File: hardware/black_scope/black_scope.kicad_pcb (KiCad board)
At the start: 4 copper layers, 87 x 59 mm, 73 parts, among them J1 Conn_ARM_JTAG_SWD_10, J3 Conn_01x02, J4 Conn_02x04_Odd_Even, J5 Conn_02x02_Odd_Even, P1 USB_C_Plug_USB2.0, Q1 S8050, SW1 SW_Push, SW2 SW_Push, U1 MCP73831-2-OT, U2 XC6206PxxxMR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

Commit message: - Added images
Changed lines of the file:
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@@
   (gr_rect (start 100 75) (end 183 130) (layer "B.SilkS") (width 0.15) (fill none))
   (gr_rect (start 183 75) (end 167 130) (layer "B.SilkS") (width 0.15) (fill none))
+  (gr_rect (start 185 79) (end 151 132) (layer "F.SilkS") (width 0.15) (fill none))
+  (gr_circle (center 181 77) (end 179 77) (layer "F.SilkS") (width 0.15) (fill none))
+  (gr_rect (start 120.5 115) (end 131.5 119) (layer "F.SilkS") (width 0.15) (fill none))
+  (gr_circle (center 161 77) (end 159 77) (layer "F.SilkS") (width 0.15) (fill none))
+  (gr_circle (center 149 84) (end 147 84) (layer "F.SilkS") (width 0.15) (fill none))
+  (gr_rect (start 124.5 115) (end 127.5 120) (layer "F.SilkS") (width 0.15) (fill none))
+  (gr_circle (center 149 119) (end 147 119) (layer "F.SilkS") (width 0.15) (fill none))
   (gr_line (start 185 130) (end 185 126) (layer "Edge.Cuts") (width 0.1))
   (gr_arc (start 185 130) (mid 184.414214 131.414214) (end 183 132) (layer "Edge.Cuts") (width 0.1))

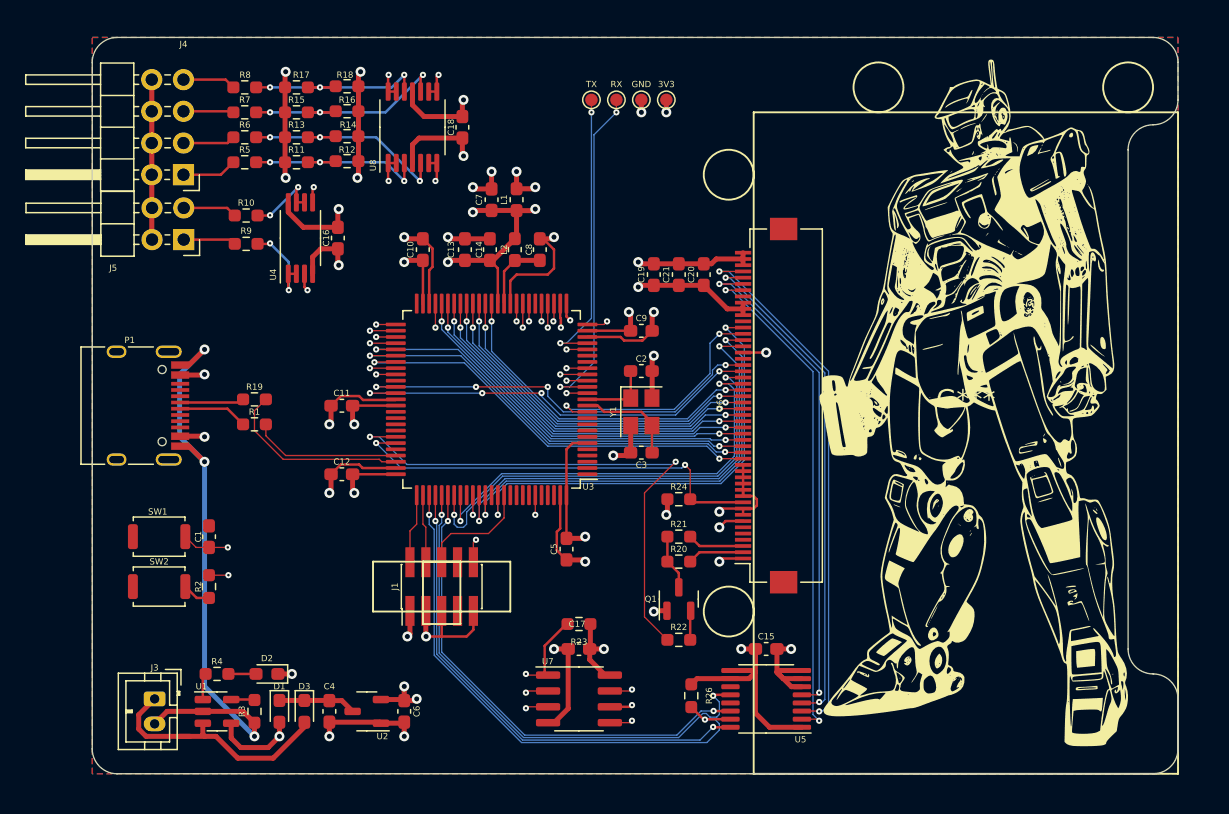
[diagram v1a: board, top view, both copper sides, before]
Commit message: - Fix PCB issues - Add datasheets
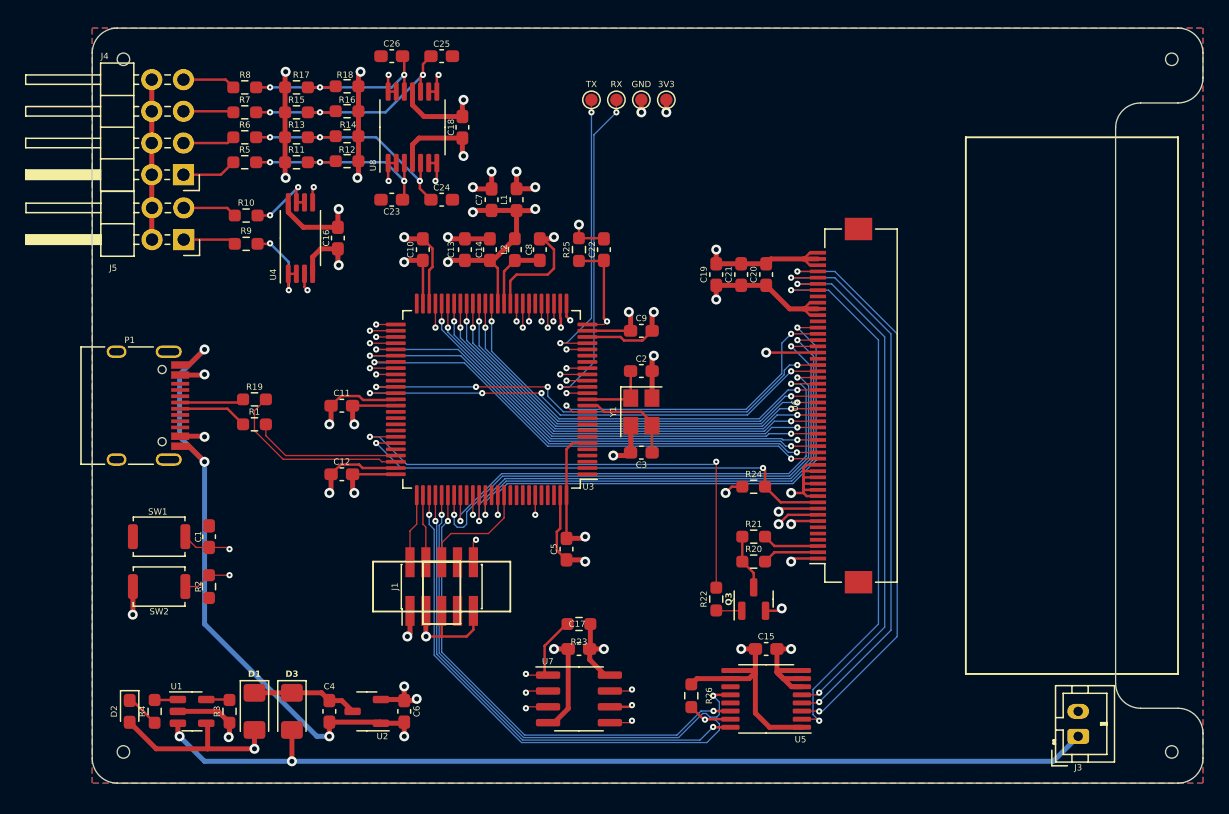
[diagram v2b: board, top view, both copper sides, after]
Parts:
- removed G***: LOGO, LOGO
- removed Q1: S8050, Package_TO_SOT_SMD:SOT-23
- added C22: 100n, Capacitor_SMD:C_0603_1608Metric_Pad1.08x0.95mm_HandSolder, F.Cu at (139.0, 90.0)
- added C23: 100p, Capacitor_SMD:C_0603_1608Metric_Pad1.08x0.95mm_HandSolder, F.Cu at (122.0, 86.0)
- added C24: 100p, Capacitor_SMD:C_0603_1608Metric_Pad1.08x0.95mm_HandSolder, F.Cu at (126.0, 86.0)
- added C25: 100p, Capacitor_SMD:C_0603_1608Metric_Pad1.08x0.95mm_HandSolder, F.Cu at (126.0, 74.5)
- added C26: 100p, Capacitor_SMD:C_0603_1608Metric_Pad1.08x0.95mm_HandSolder, F.Cu at (122.0, 74.5)
- added Q3: Q_NPN_BEC, Package_TO_SOT_SMD:SOT-23, F.Cu at (151.0, 118.0)
- added R25: 10k, Resistor_SMD:R_0603_1608Metric_Pad0.98x0.95mm_HandSolder, F.Cu at (137.0, 90.0)
- C1, C10, C11, C12, C13, C14, C15, C16, C17, C18, C19, C20, C21, C5, C9: value C -> 100n
- C2, C3: value C -> 10p
- C4, C6, C7, C8: value C -> 270n
- D1, D3: footprint Diode_SMD:D_0603_1608Metric_Pad1.05x0.95mm_HandSolder -> Diode_SMD:D_1206_3216Metric_Pad1.42x1.75mm_HandSolder
- L1, L2: value L -> 47u
- R1, R19: value R -> 22
- R10, R20, R21, R9: value R -> 51
- R11, R13, R15, R17: value R -> 2k7
- R12, R14, R16, R18: value R -> 4k3
- R2, R23, R24, R26: value R -> 10k
- R22, R4: value R -> 1k
- R3: value R -> 6.8k
- R5, R6, R7, R8: value R -> 8k2
- moved J3 74.1 mm to (177.0, 129.0), turned to 90 degrees
- moved D2 11.4 mm to (101.0, 127.0), turned to -90 degrees
- moved R24 6.08 mm to (151.0, 109.0)
- moved R20 6.00 mm to (151.0, 115.0)
- moved R21 6.00 mm to (151.0, 113.0)
- moved U6 6.00 mm to (158.0, 102.5)
- moved R4 5.83 mm to (103.0, 127.0), turned to -90 degrees
- moved C19 5.00 mm to (148.0, 92.0)
- moved C20 5.00 mm to (152.0, 92.0)
- moved C21 5.00 mm to (150.0, 92.0)
- moved R22 4.44 mm to (148.0, 118.0), turned to 90 degrees
- moved D1 2.00 mm to (111.0, 127.0)
- moved R3 2.00 mm to (109.0, 127.0)
- moved U1 2.00 mm to (106.0, 127.0)
- moved D3 1.00 mm to (114.0, 127.0)
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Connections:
- D2 pad 1: GND -> Net-(D2-K)
- D2 pad 2: Net-(D2-Pad2) -> VBUS
- R2 pad 1: Net-(R2-Pad1) -> GND
- R4 pad 1: Net-(D2-Pad2) -> Net-(U1-STAT)
- R4 pad 2: Net-(R4-Pad2) -> Net-(D2-K)
- SW2 pad 1: GND -> BOOT0
- SW2 pad 2: Net-(R2-Pad1) -> +3.3V
- U1 pad 1: Net-(R4-Pad2) -> Net-(U1-STAT)
- U6 pad 7: +3.3V -> GND
- U6 pad 8: GND -> +3.3V
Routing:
- net +BATT: track 20.5 -> 77.3 mm, vias 0 -> 2
- net GND: track 201.6 -> 216.3 mm, vias 30 -> 32
- net DAC2_OUT1: track 34.8 -> 41.8 mm
- net +3.3V: track 81.6 -> 88.1 mm, vias 16 -> 17
- net VBUS: track 43.8 -> 50.1 mm
- net FMC_D2: track 36.3 -> 42.3 mm
- net FMC_D14: track 35.2 -> 41.2 mm
- net FMC_A0: track 20.1 -> 26.1 mm
- net FMC_D7: track 28.2 -> 34.2 mm
- net FMC_D6: track 27.8 -> 33.8 mm
- net FMC_D4: track 27.2 -> 33.2 mm
- net FMC_WR: track 36.1 -> 42.1 mm
- net FMC_RD: track 37.3 -> 43.3 mm
- net FMC_D9: track 28.8 -> 34.8 mm
- net FMC_D8: track 28.5 -> 34.5 mm
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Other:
- board size 87 x 59 mm -> 89 x 60.5 mm

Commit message: - Gerber files v2
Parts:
- added C27: 100n, Capacitor_SMD:C_0603_1608Metric_Pad1.08x0.95mm_HandSolder, F.Cu at (159.0, 123.0)
- added C28: 100n, Capacitor_SMD:C_0603_1608Metric_Pad1.08x0.95mm_HandSolder, F.Cu at (159.0, 125.0)
- added C29: 100n, Capacitor_SMD:C_0603_1608Metric_Pad1.08x0.95mm_HandSolder, F.Cu at (159.0, 127.0)
- added C30: 100n, Capacitor_SMD:C_0603_1608Metric_Pad1.08x0.95mm_HandSolder, F.Cu at (159.0, 129.0)
- added D4: D_Schottky_Dual_CommonCathode_AAK_Parallel, Package_TO_SOT_SMD:SOT-23, F.Cu at (112.5, 126.7)
- added G***: LOGO, LOGO, F.Cu at (170.0, 86.0)
- added J2: Conn_02x06_Odd_Even, Connector_PinHeader_2.54mm:PinHeader_2x06_P2.54mm_Vertical_SMD, F.Cu at (104.1, 82.8)
- moved J3 1.83 mm to (175.5, 128.0), turned to 0 degrees
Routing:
- net QSPI_NSS: track 31.4 -> 55.6 mm
- net QSPI_IO1: track 32.9 -> 49.7 mm
- net QSPI_IO2: track 33.2 -> 49.8 mm
- net GND: track 216.3 -> 229.5 mm, vias 32 -> 36
- net QSPI_IO3: track 38.9 -> 49.8 mm
- net QSPI_IO0: track 38.9 -> 49.8 mm
- net YN: track 42.5 -> 45.8 mm
- net QSPI_SCLK: track 47.4 -> 49.9 mm
- net XP: track 45.1 -> 47.5 mm
- net XN: track 45.3 -> 47.7 mm
- net YP: track 46.1 -> 48.1 mm
- net VBUS: track 50.1 -> 51.8 mm
- net +BATT: track 77.3 -> 76.2 mm
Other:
- board text added: "+ -"

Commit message: Long time update
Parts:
- added C31: 270n, Capacitor_SMD:C_0603_1608Metric_Pad1.08x0.95mm_HandSolder, F.Cu at (150.3, 78.9)
- added C32: 270n, Capacitor_SMD:C_0603_1608Metric_Pad1.08x0.95mm_HandSolder, F.Cu at (144.3, 78.9)
- added L3: 47u, Inductor_SMD:L_0603_1608Metric_Pad1.05x0.95mm_HandSolder, F.Cu at (141.3, 76.9)
- added R27: 27, Resistor_SMD:R_0603_1608Metric_Pad0.98x0.95mm_HandSolder, F.Cu at (143.5, 125.5)
- added R28: 27, Resistor_SMD:R_0603_1608Metric_Pad0.98x0.95mm_HandSolder, F.Cu at (143.5, 124.0)
- added R29: 27, Resistor_SMD:R_0603_1608Metric_Pad0.98x0.95mm_HandSolder, F.Cu at (143.5, 128.5)
- added R30: 27, Resistor_SMD:R_0603_1608Metric_Pad0.98x0.95mm_HandSolder, F.Cu at (143.5, 127.0)
- added TP5: TestPoint, TestPoint:TestPoint_Pad_D1.0mm, F.Cu at (136.0, 83.5)
- added TP6: TestPoint, TestPoint:TestPoint_Pad_D1.0mm, F.Cu at (134.0, 83.5)
- added U9: XC6206PxxxMR, Package_TO_SOT_SMD:SOT-23-3, F.Cu at (147.3, 78.9)
- R20, R21: value 51 -> 27
- moved C8 11.2 mm to (132.3, 78.9)
- moved L1 11.1 mm to (141.3, 79.9), turned to 180 degrees
- moved C7 10.9 mm to (138.3, 78.9)
- moved L2 10.7 mm to (135.3, 79.9), turned to 180 degrees
- moved TP1 9.86 mm to (143.0, 86.5)
- moved TP2 9.86 mm to (145.0, 86.5)
- moved TP3 9.86 mm to (147.0, 86.5)
- moved TP4 9.86 mm to (149.0, 86.5)
- moved U6 1.00 mm to (159.0, 102.5)
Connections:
- C13 pad 2: GND -> GNDA
- C14 pad 2: GND -> GNDA
- C16 pad 2: GND -> GNDA
- C18 pad 2: GND -> GNDA
- C22 pad 2: GND -> GNDA
- C23 pad 2: GND -> GNDA
- C24 pad 2: GND -> GNDA
- C25 pad 2: GND -> GNDA
- C26 pad 2: GND -> GNDA
- C7 pad 2: GND -> GNDA
- C8 pad 2: GND -> GNDA
- J2 pad 10: unconnected-(J2-Pin_10-Pad10) -> GNDA
- J2 pad 12: unconnected-(J2-Pin_12-Pad12) -> GNDA
- J2 pad 2: unconnected-(J2-Pin_2-Pad2) -> GNDA
- J2 pad 4: unconnected-(J2-Pin_4-Pad4) -> GNDA
- J2 pad 6: unconnected-(J2-Pin_6-Pad6) -> GNDA
- J2 pad 8: unconnected-(J2-Pin_8-Pad8) -> GNDA
- J4 pad 2: GND -> GNDA
- J4 pad 4: GND -> GNDA
- J4 pad 6: GND -> GNDA
- J4 pad 8: GND -> GNDA
- J5 pad 2: GND -> GNDA
- J5 pad 4: GND -> GNDA
- L1 pad 1: +3.3V -> Net-(U9-VO)
- R12 pad 1: GND -> GNDA
- R14 pad 1: GND -> GNDA
- R16 pad 1: GND -> GNDA
- R18 pad 1: GND -> GNDA
- R25 pad 1: GND -> GNDA
- R26 pad 2: SPI3_NSS -> Net-(U5-~{CS})
- U3 pad 35: GND -> GNDA
- U4 pad 4: GND -> GNDA
- U5 pad 12: SPI3_MISO -> Net-(U5-DOUT)
- U5 pad 14: SPI3_MOSI -> Net-(U5-DIN)
- U5 pad 15: SPI3_NSS -> Net-(U5-~{CS})
- U5 pad 16: SPI3_SCLK -> Net-(U5-DCLK)
- U8 pad 11: GND -> GNDA
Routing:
- net Net-(D1-K): track 8.50 -> 127.2 mm, vias 0 -> 5
- net GNDA: track 0.00 -> 78.0 mm, vias 0 -> 81
- net GND: track 229.5 -> 198.1 mm, vias 36 -> 30
- net VREF: track 5.81 -> 20.2 mm, vias 0 -> 3
- net SPI3_NSS: track 44.7 -> 35.6 mm
- net UART1_RX: track 27.5 -> 21.0 mm
- net +3.3VA: track 39.8 -> 45.7 mm, vias 7 -> 13
- net UART1_TX: track 23.0 -> 17.2 mm
- net Net-(U5-DOUT): track 0.00 -> 5.63 mm
- net Net-(U5-~{CS}): track 0.00 -> 5.27 mm
- net Net-(U5-DIN): track 0.00 -> 5.25 mm
- net SPI3_SCLK: track 39.6 -> 34.8 mm
- net Net-(U5-DCLK): track 0.00 -> 4.82 mm
- net Net-(U9-VO): track 0.00 -> 4.08 mm
- net SPI3_MOSI: track 39.5 -> 36.2 mm
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- added copper zone on In2.Cu, net +3.3V
- added copper zone on In1.Cu, net +3.3VA
- added copper zone on B.Cu, net GNDA
- added copper zone on F.Cu, net GNDA
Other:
- board text added: "move 1 mm"
